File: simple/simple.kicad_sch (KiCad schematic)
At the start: 2 parts, among them J1 Screw_Terminal_01x02, U1 RPMH3.3-1.5

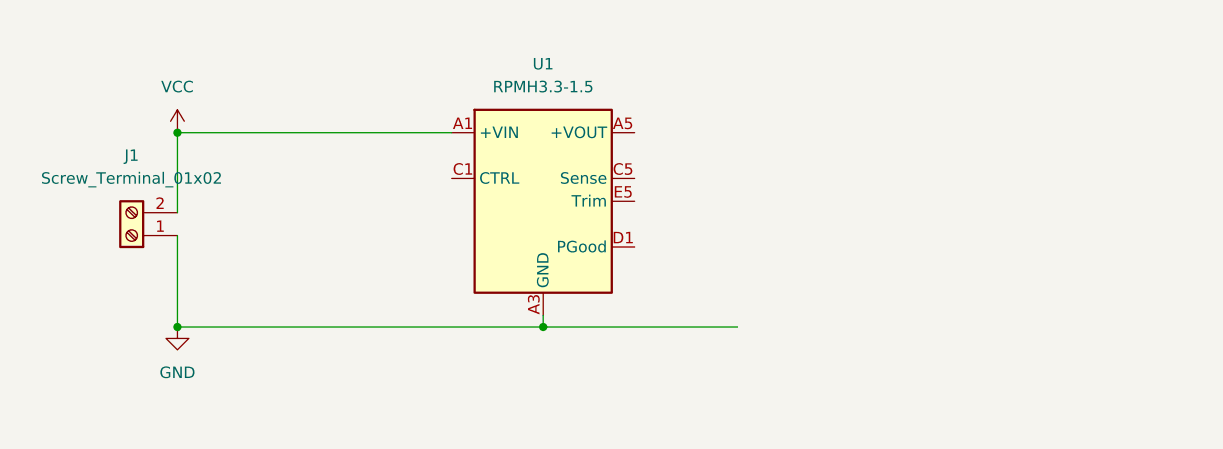
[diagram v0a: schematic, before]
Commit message: connect output and make ERC happy
Signed-off-by: Per Hallsmark <per@hallsmark.se>
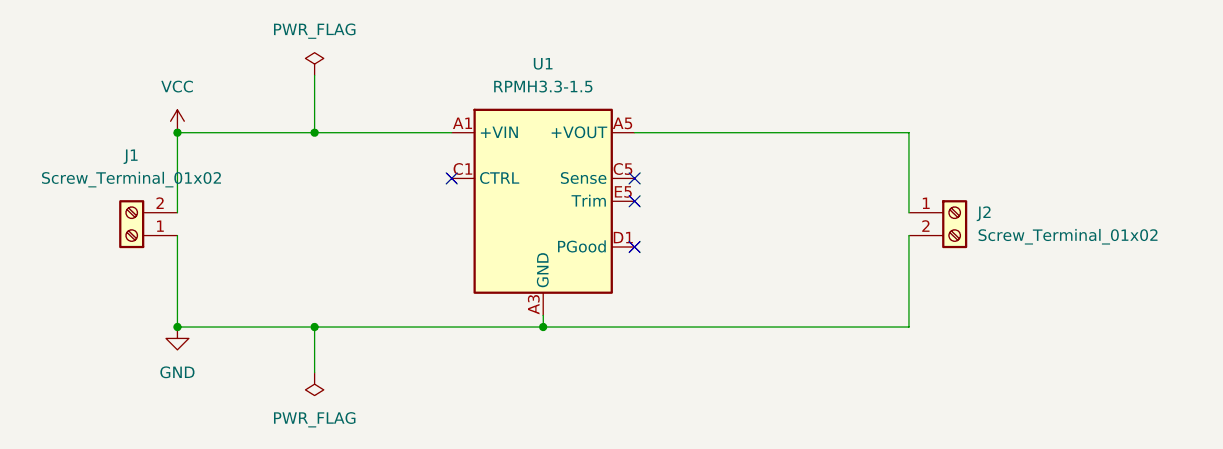
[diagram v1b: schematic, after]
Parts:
- added J2: Screw_Terminal_01x02, symbol Connector:Screw_Terminal_01x02
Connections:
- net GND: now also J2.2 (Pin_2)
- net at U1.A5 (+VOUT), U1.B5 (+VOUT): now also J2.1 (Pin_1)
- no-connect marks 0 -> 4
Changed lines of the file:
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@@
   (junction (at 36.83 100.33) (diameter 0) (color 0 0 0 0)
   )
+  (junction (at 52.07 100.33) (diameter 0) (color 0 0 0 0)
+  )
   (junction (at 36.83 78.74) (diameter 0) (color 0 0 0 0)
   )
+  (junction (at 52.07 78.74) (diameter 0) (color 0 0 0 0)
+  )
   (junction (at 77.47 100.33) (diameter 0) (color 0 0 0 0)
   )
-  (wire (pts (xy 77.47 100.33) (xy 99.06 100.33))
-    (stroke (width 0) (type default))
-  )
-  (wire (pts (xy 36.83 78.74) (xy 67.31 78.74))
+  (no_connect (at 87.63 86.36))
+  (no_connect (at 87.63 91.44))
+  (no_connect (at 87.63 83.82))
+  (no_connect (at 67.31 83.82))
+  (wire (pts (xy 52.07 100.33) (xy 77.47 100.33))
+    (stroke (width 0) (type default))
+  )
+  (wire (pts (xy 118.11 100.33) (xy 118.11 90.17))
+    (stroke (width 0) (type default))
+  )
+  (wire (pts (xy 118.11 78.74) (xy 118.11 87.63))
+    (stroke (width 0) (type default))
+  )
+  (wire (pts (xy 52.07 78.74) (xy 67.31 78.74))
+    (stroke (width 0) (type default))
+  )
+  (wire (pts (xy 52.07 72.39) (xy 52.07 78.74))
+    (stroke (width 0) (type default))
+  )
+  (wire (pts (xy 52.07 100.33) (xy 52.07 105.41))
+    (stroke (width 0) (type default))
+  )
+  (wire (pts (xy 77.47 100.33) (xy 118.11 100.33))
+    (stroke (width 0) (type default))
+  )
+  (wire (pts (xy 36.83 78.74) (xy 52.07 78.74))
     (stroke (width 0) (type default))
   )
@@
     (stroke (width 0) (type default))
   )
-  (wire (pts (xy 36.83 100.33) (xy 77.47 100.33))
+  (wire (pts (xy 36.83 100.33) (xy 52.07 100.33))
+    (stroke (width 0) (type default))
+  )
+  (wire (pts (xy 87.63 78.74) (xy 118.11 78.74))
     (stroke (width 0) (type default))
   )
@@
     )
   )
+  (symbol (lib_id "Connector:Screw_Terminal_01x02") (at 123.19 87.63 0) (unit 1)
+    (in_bom yes) (on_board yes) (dnp no) (fields_autoplaced)
+    (property "Reference" "J2" (at 125.73 87.63 0)
+      (effects (font (size 1.27 1.27)) (justify left))
+    )
+    (property "Value" "Screw_Terminal_01x02" (at 125.73 90.17 0)
+      (effects (font (size 1.27 1.27)) (justify left))
+    )
+    (property "Footprint" "" (at 123.19 87.63 0)
+      (effects (font (size 1.27 1.27)) hide)
+    )
+    (property "Datasheet" "~" (at 123.19 87.63 0)
+      (effects (font (size 1.27 1.27)) hide)
+    )
+    (pin "1")
+    (pin "2")
+    (instances
+      (project "simple"
+        (path "/811f7822-4cec-430f-a1d6-2c346407fe4c"
+          (reference "J2") (unit 1)
+        )
+      )
+    )
+  )
   (symbol (lib_id "power:GND") (at 36.83 100.33 0) (unit 1)
     (in_bom yes) (on_board yes) (dnp no) (fields_autoplaced)
@@
         )
       )
+    )
+  )
+  (symbol (lib_id "power:PWR_FLAG") (at 52.07 105.41 180) (unit 1)
+    (in_bom yes) (on_board yes) (dnp no) (fields_autoplaced)
+    (property "Reference" "#FLG02" (at 52.07 107.315 0)
+      (effects (font (size 1.27 1.27)) hide)
+    )
+    (property "Value" "PWR_FLAG" (at 52.07 110.49 0)
+      (effects (font (size 1.27 1.27)))
+    )
+    (property "Footprint" "" (at 52.07 105.41 0)
+      (effects (font (size 1.27 1.27)) hide)
+    )
+    (property "Datasheet" "~" (at 52.07 105.41 0)
+      (effects (font (size 1.27 1.27)) hide)
+    )
+    (pin "1")
+    (instances
+      (project "simple"
+        (path "/811f7822-4cec-430f-a1d6-2c346407fe4c"
+          (reference "#FLG02") (unit 1)
+        )
+      )
+    )
+  )
+  (symbol (lib_id "power:PWR_FLAG") (at 52.07 72.39 0) (unit 1)
+    (in_bom yes) (on_board yes) (dnp no) (fields_autoplaced)
+    (property "Reference" "#FLG01" (at 52.07 70.485 0)
+      (effects (font (size 1.27 1.27)) hide)
+    )
+    (property "Value" "PWR_FLAG" (at 52.07 67.31 0)
+      (effects (font (size 1.27 1.27)))
+    )
+    (property "Footprint" "" (at 52.07 72.39 0)
+      (effects (font (size 1.27 1.27)) hide)
+    )
+    (property "Datasheet" "~" (at 52.07 72.39 0)
+      (effects (font (size 1.27 1.27)) hide)
+    )
+    (pin "1")
+    (instances
+      (project "simple"
+        (path "/811f7822-4cec-430f-a1d6-2c346407fe4c"
+          (reference "#FLG01") (unit 1)
+        )
+      )
